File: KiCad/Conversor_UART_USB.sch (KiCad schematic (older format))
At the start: 5 parts

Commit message: pble_zip
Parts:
- C_Reset_Conversor1: footprint (none) -> Capacitor_Tantalum_SMD:CP_EIA-6032-28_Kemet-C_Pad2.25x2.35mm_HandSolder
- Cref0, Cref1: footprint (none) -> Capacitor_Tantalum_SMD:CP_EIA-3216-18_Kemet-A_Pad1.58x1.35mm_HandSolder
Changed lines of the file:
@@
 F 0 "C_Reset_Conversor1" H 2665 2796 50  0000 L CNN
 F 1 "1uF" H 2665 2705 50  0000 L CNN
-F 2 "" H 2550 2750 50  0001 C CNN
+F 2 "Capacitor_Tantalum_SMD:CP_EIA-6032-28_Kemet-C_Pad2.25x2.35mm_HandSolder" H 2550 2750 50  0001 C CNN
 F 3 "~" H 2550 2750 50  0001 C CNN
 	1    2550 2750
@@
 F 0 "Cref0" V 5040 2250 50  0000 C CNN
 F 1 "10uF" V 5039 2250 50  0001 C BNN
-F 2 "" H 5238 2100 50  0001 C CNN
+F 2 "Capacitor_Tantalum_SMD:CP_EIA-3216-18_Kemet-A_Pad1.58x1.35mm_HandSolder" H 5238 2100 50  0001 C CNN
 F 3 "~" H 5200 2250 50  0001 C CNN
 	1    5200 2250
@@
 F 0 "Cref1" V 5040 1950 50  0000 C CNN
 F 1 "10uF" V 5039 1950 50  0001 C CNN
-F 2 "" H 5238 1800 50  0001 C CNN
+F 2 "Capacitor_Tantalum_SMD:CP_EIA-3216-18_Kemet-A_Pad1.58x1.35mm_HandSolder" H 5238 1800 50  0001 C CNN
 F 3 "~" H 5200 1950 50  0001 C CNN
 	1    5200 1950

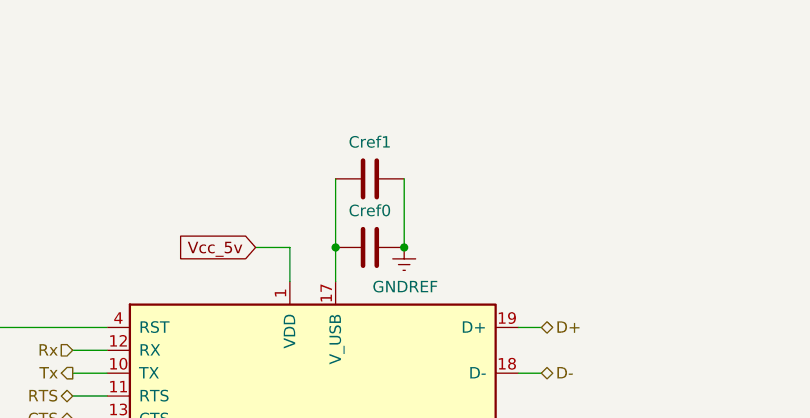
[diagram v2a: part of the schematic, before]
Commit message: correção P1: LCD e Capacitores
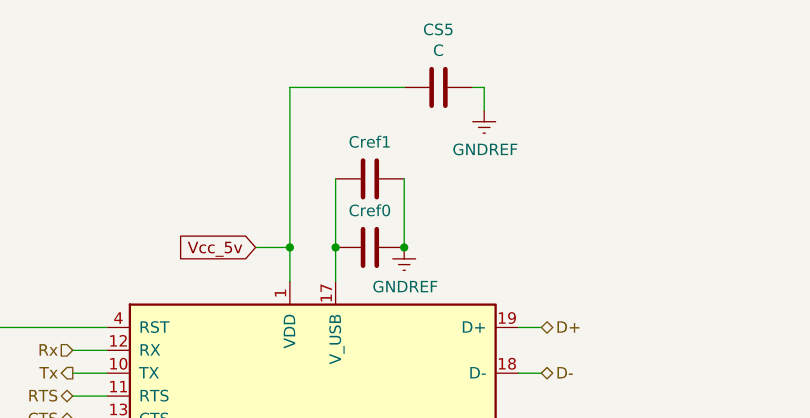
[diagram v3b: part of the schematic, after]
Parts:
- added CS5: C, Capacitor_SMD:C_0805_2012Metric_Pad1.18x1.45mm_HandSolder, symbol Device:C
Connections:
- net GNDREF: now also CS5.1
- net Vcc_5v: now also CS5.2
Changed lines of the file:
@@
 Text GLabel 4700 2250 0    50   Input ~ 0
 Vcc_5v
+$Comp
+L power:GNDREF #PWR?
+U 1 1 60FB0F70
+P 5700 1650
+AR Path="/60FB0F70" Ref="#PWR?"  Part="1"
+AR Path="/60BE4F2F/60FB0F70" Ref="#PWR06"  Part="1"
+F 0 "#PWR06" H 5700 1400 50  0001 C CNN
+F 1 "GNDREF" H 5705 1477 50  0000 C CNN
+F 2 "" H 5700 1650 50  0001 C CNN
+F 3 "" H 5700 1650 50  0001 C CNN
+	1    5700 1650
+	1    0    0    -1
+$EndComp
+$Comp
+L Device:C CS?
+U 1 1 60FB0F76
+P 5500 1550
+AR Path="/60FB0F76" Ref="CS?"  Part="1"
+AR Path="/60BE4F2F/60FB0F76" Ref="CS5"  Part="1"
+F 0 "CS5" V 5248 1550 50  0000 C CNN
+F 1 "C" V 5339 1550 50  0000 C CNN
+F 2 "Capacitor_SMD:C_0805_2012Metric_Pad1.18x1.45mm_HandSolder" H 5538 1400 50  0001 C CNN
+F 3 "~" H 5500 1550 50  0001 C CNN
+	1    5500 1550
+	0    1    1    0
+$EndComp
+Wire Wire Line
+	5700 1650 5700 1550
+Wire Wire Line
+	5700 1550 5650 1550
+Wire Wire Line
+	5350 1550 4850 1550
+Wire Wire Line
+	4850 1550 4850 2250
+Connection ~ 4850 2250
 $EndSCHEMATC

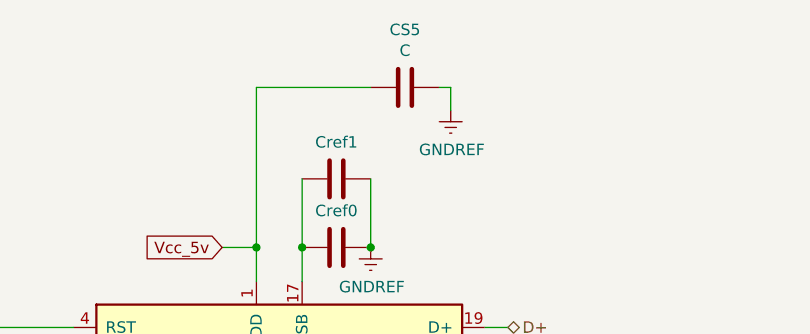
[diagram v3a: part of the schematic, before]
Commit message: Valores dos capacitores CS
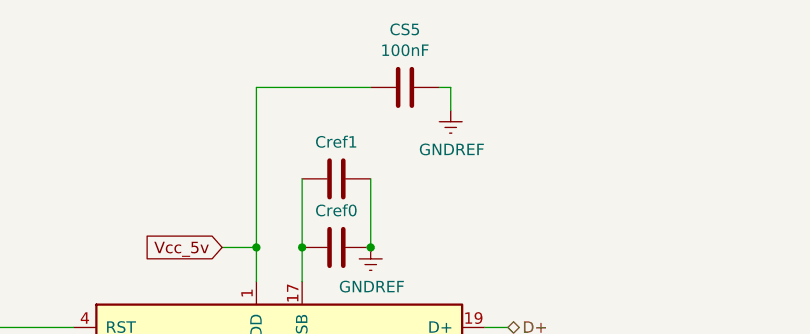
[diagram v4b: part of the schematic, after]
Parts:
- CS5: value C -> 100nF
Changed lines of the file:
@@
 AR Path="/60BE4F2F/60FB0F76" Ref="CS5"  Part="1"
 F 0 "CS5" V 5248 1550 50  0000 C CNN
-F 1 "C" V 5339 1550 50  0000 C CNN
+F 1 "100nF" V 5339 1550 50  0000 C CNN
 F 2 "Capacitor_SMD:C_0805_2012Metric_Pad1.18x1.45mm_HandSolder" H 5538 1400 50  0001 C CNN
 F 3 "~" H 5500 1550 50  0001 C CNN
